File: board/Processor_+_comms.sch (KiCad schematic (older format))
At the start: 38 parts, among them U11 ATXMEGA256A3U-MH, U12 NTS0104, U14 TC1015-3.3VCT713

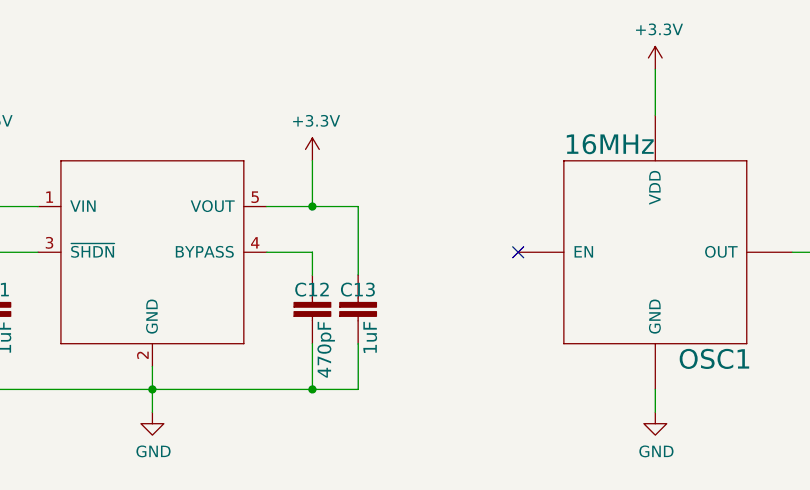
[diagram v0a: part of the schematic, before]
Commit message: Added testpoints and fixed up some issues with footprints etc
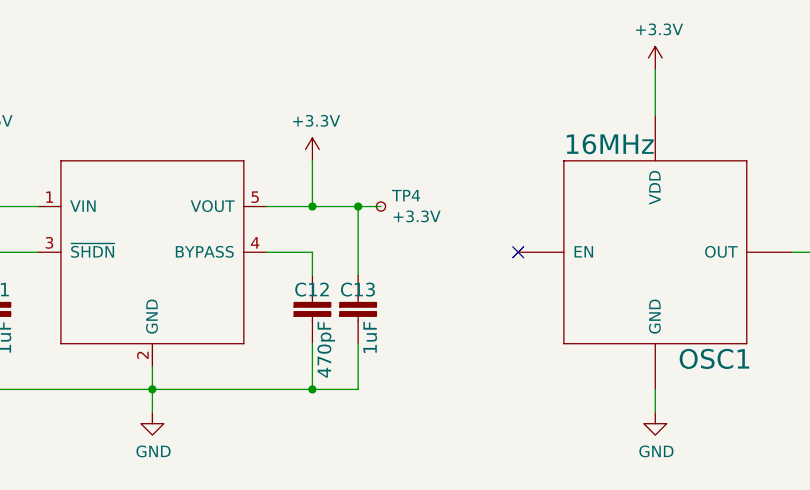
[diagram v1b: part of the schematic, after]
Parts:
- added TP4: +3.3V, TestPoint:TestPoint_Pad_D1.5mm, symbol Connector:TestPoint_Small
- C11, C13: URL https://uk.farnell.com/multicomp/mc0603x105k100ct/cap-1-f-1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 -> (none); URL_FARNELL (none) -> https://uk.farnell.com/multicomp/mc0603x105k100ct/cap-1-f-1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
- C12: URL https://uk.farnell.com/multicomp/mc0603b471j500ct/cap-470pf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 -> (none); URL_FARNELL (none) -> https://uk.farnell.com/multicomp/mc0603b471j500ct/cap-470pf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
- OSC1: URL http://uk.farnell.com/iqd-frequency-products/lfspxo025494/o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 -> (none); URL_FARNELL (none) -> http://uk.farnell.com/iqd-frequency-products/lfspxo025494/o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
- R17, R19: URL https://uk.farnell.com/vishay/crcw08051m00fkea/res-1m-1-0-1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 -> (none); URL_FARNELL (none) -> https://uk.farnell.com/vishay/crcw08051m00fkea/res-1m-1-0-1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
- U14: footprint MXKeyboard_RGB:SOT23-5L -> Package_TO_SOT_SMD:SOT-23-5
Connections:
- net +3V3: now also TP4.1
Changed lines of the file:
@@
 F 5 "CRCW08051M00FKEA" H 9700 5950 59  0001 L BNN "MPN"
 F 6 "1652946" H 9700 5950 59  0001 L BNN "OC_FARNELL"
-F 7 "https://uk.farnell.com/vishay/crcw08051m00fkea/res-1m-1-0-125w-0805-thick-film/dp/1652946" H 9700 5950 59  0001 L BNN "URL"
+F 7 "" H 9700 5950 59  0001 L BNN "URL"
+F 8 "https://uk.farnell.com/vishay/crcw08051m00fkea/res-1m-1-0-125w-0805-thick-film/dp/1652946" H 9700 5950 50  0001 C CNN "URL_FARNELL"
 	1    9700 5950
 	0    -1   -1   0
@@
 F 5 "CRCW08051M00FKEA" H 14300 7400 59  0001 L BNN "MPN"
 F 6 "1652946" H 14300 7400 59  0001 L BNN "OC_FARNELL"
-F 7 "https://uk.farnell.com/vishay/crcw08051m00fkea/res-1m-1-0-125w-0805-thick-film/dp/1652946" H 14300 7400 59  0001 L BNN "URL"
+F 7 "" H 14300 7400 59  0001 L BNN "URL"
+F 8 "https://uk.farnell.com/vishay/crcw08051m00fkea/res-1m-1-0-125w-0805-thick-film/dp/1652946" H 14300 7400 50  0001 C CNN "URL_FARNELL"
 	1    14300 7400
 	1    0    0    -1
@@
 F 0 "U14" H 7700 2200 50  0001 C CNN
 F 1 "TC1015-3.3VCT713" H 7700 2200 50  0001 C CNN
-F 2 "MXKeyboard_RGB:SOT23-5L" H 7700 2200 50  0001 C CNN
+F 2 "Package_TO_SOT_SMD:SOT-23-5" H 7700 2200 50  0001 C CNN
 F 3 "" H 7700 2200 50  0001 C CNN
 	1    7700 2200
@@
 F 5 "MC0603X105K100CT" H 7000 2400 59  0001 L BNN "MPN"
 F 6 "1759399" H 7000 2400 59  0001 L BNN "OC_FARNELL"
-F 7 "https://uk.farnell.com/multicomp/mc0603x105k100ct/cap-1-f-10v-10-x5r-0603/dp/1759399" H 7000 2400 59  0001 L BNN "URL"
+F 7 "" H 7000 2400 59  0001 L BNN "URL"
+F 8 "https://uk.farnell.com/multicomp/mc0603x105k100ct/cap-1-f-10v-10-x5r-0603/dp/1759399" H 7000 2400 50  0001 C CNN "URL_FARNELL"
 	1    7000 2400
 	1    0    0    -1
@@
 F 5 "MC0603B471J500CT" H 8400 2400 59  0001 L BNN "MPN"
 F 6 "2627442" H 8400 2400 59  0001 L BNN "OC_FARNELL"
-F 7 "https://uk.farnell.com/multicomp/mc0603b471j500ct/cap-470pf-50v-5-x7r-0603/dp/2627442" H 8400 2400 59  0001 L BNN "URL"
+F 7 "" H 8400 2400 59  0001 L BNN "URL"
+F 8 "https://uk.farnell.com/multicomp/mc0603b471j500ct/cap-470pf-50v-5-x7r-0603/dp/2627442" H 8400 2400 50  0001 C CNN "URL_FARNELL"
 	1    8400 2400
 	1    0    0    -1
@@
 F 5 "MC0603X105K100CT" H 8600 2400 59  0001 L BNN "MPN"
 F 6 "1759399" H 8600 2400 59  0001 L BNN "OC_FARNELL"
-F 7 "https://uk.farnell.com/multicomp/mc0603x105k100ct/cap-1-f-10v-10-x5r-0603/dp/1759399" H 8600 2400 59  0001 L BNN "URL"
+F 7 "" H 8600 2400 59  0001 L BNN "URL"
+F 8 "https://uk.farnell.com/multicomp/mc0603x105k100ct/cap-1-f-10v-10-x5r-0603/dp/1759399" H 8600 2400 50  0001 C CNN "URL_FARNELL"
 	1    8600 2400
 	1    0    0    -1
@@
 F 9 "LFSPXO025494" H 9900 2200 85  0001 L BNN "MPN"
 F 10 "2449455" H 9900 2200 85  0001 L BNN "OC_FARNELL"
-F 11 "http://uk.farnell.com/iqd-frequency-products/lfspxo025494/oscillator-16mhz-15pf-smd/dp/2449455" H 9900 2200 85  0001 L BNN "URL"
+F 11 "" H 9900 2200 85  0001 L BNN "URL"
+F 12 "http://uk.farnell.com/iqd-frequency-products/lfspxo025494/oscillator-16mhz-15pf-smd/dp/2449455" H 9900 2200 50  0001 C CNN "URL_FARNELL"
 	1    9900 2200
 	1    0    0    -1
@@
 	-1   0    0    1
 $EndComp
+$Comp
+L Connector:TestPoint_Small TP4
+U 1 1 5F711D45
+P 8700 2000
+F 0 "TP4" H 8748 2046 50  0000 L CNN
+F 1 "+3.3V" H 8748 1955 50  0000 L CNN
+F 2 "TestPoint:TestPoint_Pad_D1.5mm" H 8900 2000 50  0001 C CNN
+F 3 "~" H 8900 2000 50  0001 C CNN
+	1    8700 2000
+	1    0    0    -1
+$EndComp
+Wire Wire Line
+	8700 2000 8600 2000
+Connection ~ 8600 2000
 Wire Bus Line
 	4350 4400 4350 4800

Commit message: Updated the footprints in the schematic having renamed all of my published libraries
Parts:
- C1, C11, C12, C13, C2, C3, C4, C5, C6, C7, C8, C9: footprint rcl:C0603 -> rhais_rcl:C0603
- R17, R18, R19, R37, R38: footprint rcl:R0603 -> rhais_rcl:R0603
- U14: footprint Package_TO_SOT_SMD:SOT-23-5 -> rhais_package-smd:SOT-23-5
- USB: footprint USB:MICRO-USB-B-(IN_PCB) -> rhais_usb:MICRO-USB-B-(IN_PCB)
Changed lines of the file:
@@
 F 0 "USB1" H 10000 5550 59  0000 R CNN
 F 1 "USB" H 10000 4850 59  0000 R CNN
-F 2 "USB:MICRO-USB-B-(IN_PCB)" H 9850 5200 50  0001 C CNN
+F 2 "rhais_usb:MICRO-USB-B-(IN_PCB)" H 9850 5200 50  0001 C CNN
 F 3 "" H 9850 5200 50  0001 C CNN
 	1    9850 5200
@@
 F 0 "C1" H 10010 5915 59  0000 L BNN
 F 1 "0.1uF" H 10010 5715 59  0000 L BNN
-F 2 "rcl:C0603" H 9950 5900 50  0001 C CNN
+F 2 "rhais_rcl:C0603" H 9950 5900 50  0001 C CNN
 F 3 "" H 9950 5900 50  0001 C CNN
 F 4 "Multicomp" H 9950 5900 59  0001 L BNN "MFR"
@@
 F 0 "R17" H 9700 6000 59  0000 C BNN
 F 1 "1M" H 9700 5900 59  0000 C TNN
-F 2 "rcl:R0603" H 9700 5950 50  0001 C CNN
+F 2 "rhais_rcl:R0603" H 9700 5950 50  0001 C CNN
 F 3 "" H 9700 5950 50  0001 C CNN
 F 4 "Vishay" H 9700 5950 59  0001 L BNN "MFR"
@@
 F 0 "C2" H 5300 2100 59  0000 C BNN
 F 1 "0.1uF" V 5320 2000 59  0000 R TNN
-F 2 "rcl:C0603" H 5300 2100 50  0001 C CNN
+F 2 "rhais_rcl:C0603" H 5300 2100 50  0001 C CNN
 F 3 "" H 5300 2100 50  0001 C CNN
 F 4 "Multicomp" H 5300 2100 59  0001 L BNN "MFR"
@@
 F 0 "C3" H 5500 2100 59  0000 C BNN
 F 1 "0.1uF" V 5520 2000 59  0000 R TNN
-F 2 "rcl:C0603" H 5500 2100 50  0001 C CNN
+F 2 "rhais_rcl:C0603" H 5500 2100 50  0001 C CNN
 F 3 "" H 5500 2100 50  0001 C CNN
 F 4 "Multicomp" H 5500 2100 59  0001 L BNN "MFR"
@@
 F 0 "C4" H 5700 2100 59  0000 C BNN
 F 1 "0.1uF" V 5720 2000 59  0000 R TNN
-F 2 "rcl:C0603" H 5700 2100 50  0001 C CNN
+F 2 "rhais_rcl:C0603" H 5700 2100 50  0001 C CNN
 F 3 "" H 5700 2100 50  0001 C CNN
 F 4 "Multicomp" H 5700 2100 59  0001 L BNN "MFR"
@@
 F 0 "C5" H 5900 2100 59  0000 C BNN
 F 1 "0.1uF" V 5920 2000 59  0000 R TNN
-F 2 "rcl:C0603" H 5900 2100 50  0001 C CNN
+F 2 "rhais_rcl:C0603" H 5900 2100 50  0001 C CNN
 F 3 "" H 5900 2100 50  0001 C CNN
 F 4 "Multicomp" H 5900 2100 59  0001 L BNN "MFR"
@@
 F 0 "C6" H 6100 2100 59  0000 C BNN
 F 1 "0.1uF" V 6120 2000 59  0000 R TNN
-F 2 "rcl:C0603" H 6100 2100 50  0001 C CNN
+F 2 "rhais_rcl:C0603" H 6100 2100 50  0001 C CNN
 F 3 "" H 6100 2100 50  0001 C CNN
 F 4 "Multicomp" H 6100 2100 59  0001 L BNN "MFR"
@@
 F 0 "R18" H 4800 4150 59  0000 C BNN
 F 1 "10k" H 4800 4050 59  0000 C TNN
-F 2 "rcl:R0603" H 4800 4100 50  0001 C CNN
+F 2 "rhais_rcl:R0603" H 4800 4100 50  0001 C CNN
 F 3 "" H 4800 4100 50  0001 C CNN
 F 4 "Multicomp" H 4800 4100 59  0001 L BNN "MFR"
@@
 F 0 "R19" H 14300 7450 59  0000 C BNN
 F 1 "1M" H 14300 7350 59  0000 C TNN
-F 2 "rcl:R0603" H 14300 7400 50  0001 C CNN
+F 2 "rhais_rcl:R0603" H 14300 7400 50  0001 C CNN
 F 3 "" H 14300 7400 50  0001 C CNN
 F 4 "Vishay" H 14300 7400 59  0001 L BNN "MFR"
@@
 F 0 "C7" V 14315 7090 59  0000 L TNN
 F 1 "0.1uF" V 14315 6990 59  0000 R TNN
-F 2 "rcl:C0603" H 14250 7100 50  0001 C CNN
+F 2 "rhais_rcl:C0603" H 14250 7100 50  0001 C CNN
 F 3 "" H 14250 7100 50  0001 C CNN
 F 4 "Multicomp" H 14250 7100 59  0001 L BNN "MFR"
@@
 F 0 "C8" H 13560 5815 59  0000 L BNN
 F 1 "0.1uF" H 13560 5615 59  0000 L BNN
-F 2 "rcl:C0603" H 13500 5800 50  0001 C CNN
+F 2 "rhais_rcl:C0603" H 13500 5800 50  0001 C CNN
 F 3 "" H 13500 5800 50  0001 C CNN
 F 4 "Multicomp" H 13500 5800 59  0001 L BNN "MFR"
@@
 F 0 "C9" H 12160 5815 59  0000 L BNN
 F 1 "0.1uF" H 12160 5615 59  0000 L BNN
-F 2 "rcl:C0603" H 12100 5800 50  0001 C CNN
+F 2 "rhais_rcl:C0603" H 12100 5800 50  0001 C CNN
 F 3 "" H 12100 5800 50  0001 C CNN
 F 4 "Multicomp" H 12100 5800 59  0001 L BNN "MFR"
@@
 F 0 "U14" H 7700 2200 50  0001 C CNN
 F 1 "TC1015-3.3VCT713" H 7700 2200 50  0001 C CNN
-F 2 "Package_TO_SOT_SMD:SOT-23-5" H 7700 2200 50  0001 C CNN
+F 2 "rhais_package-smd:SOT-23-5" H 7700 2200 50  0001 C CNN
 F 3 "" H 7700 2200 50  0001 C CNN
 	1    7700 2200
@@
 F 0 "C11" H 7000 2400 59  0000 C BNN
 F 1 "1uF" V 7020 2300 59  0000 R TNN
-F 2 "rcl:C0603" H 7000 2400 50  0001 C CNN
+F 2 "rhais_rcl:C0603" H 7000 2400 50  0001 C CNN
 F 3 "" H 7000 2400 50  0001 C CNN
 F 4 "Multicomp" H 7000 2400 59  0001 L BNN "MFR"
@@
 F 0 "C12" H 8400 2400 59  0000 C BNN
 F 1 "470pF" V 8420 2300 59  0000 R TNN
-F 2 "rcl:C0603" H 8400 2400 50  0001 C CNN
+F 2 "rhais_rcl:C0603" H 8400 2400 50  0001 C CNN
 F 3 "" H 8400 2400 50  0001 C CNN
 F 4 "Multicomp" H 8400 2400 59  0001 L BNN "MFR"
@@
 F 0 "C13" H 8600 2400 59  0000 C BNN
 F 1 "1uF" V 8620 2300 59  0000 R TNN
-F 2 "rcl:C0603" H 8600 2400 50  0001 C CNN
+F 2 "rhais_rcl:C0603" H 8600 2400 50  0001 C CNN
 F 3 "" H 8600 2400 50  0001 C CNN
 F 4 "Multicomp" H 8600 2400 59  0001 L BNN "MFR"
@@
 F 0 "R37" H 9300 5800 59  0000 C BNN
 F 1 "100k" H 9300 5700 59  0000 C TNN
-F 2 "rcl:R0603" H 9300 5750 50  0001 C CNN
+F 2 "rhais_rcl:R0603" H 9300 5750 50  0001 C CNN
 F 3 "" H 9300 5750 50  0001 C CNN
 	1    9300 5750
@@
 F 0 "R38" V 9450 4500 50  0000 C BNN
 F 1 "10k" V 9550 4500 50  0000 C TNN
-F 2 "rcl:R0603" H 9500 4500 50  0001 C CNN
+F 2 "rhais_rcl:R0603" H 9500 4500 50  0001 C CNN
 F 3 "" H 9500 4500 50  0001 C CNN
 F 4 "Multicomp" H 9500 4500 50  0001 C CNN "MFR"

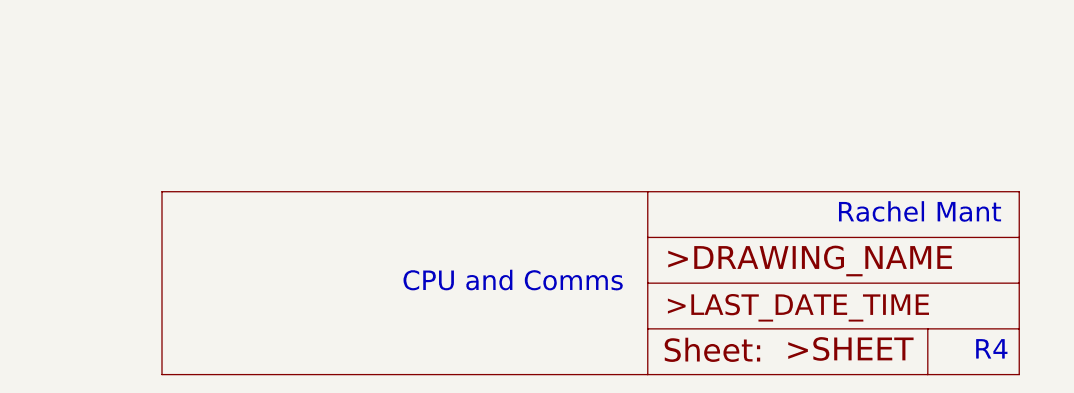
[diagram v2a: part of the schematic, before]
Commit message: Fixed up the schematics metadata to properly capture revision, block and authorship information
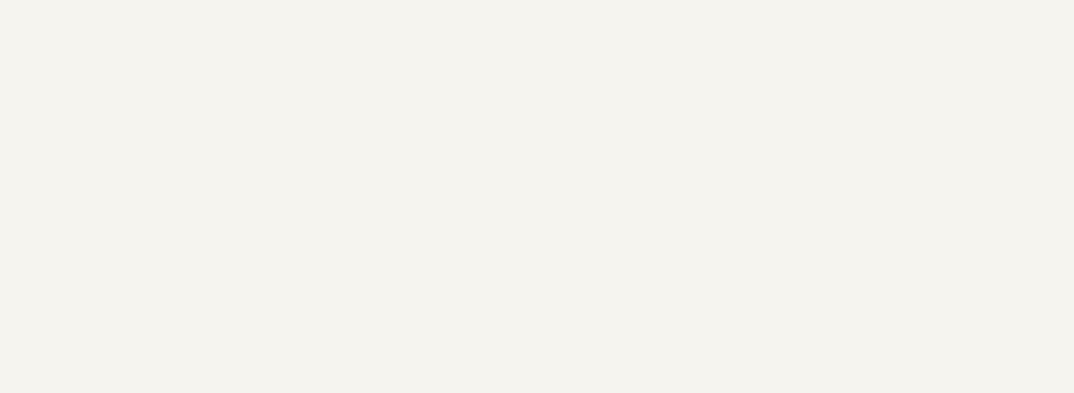
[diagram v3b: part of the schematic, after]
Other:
- note removed: "CPU and Comms"
- note removed: "R4"
- note removed: "Rachel Mant"
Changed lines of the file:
@@
 encoding utf-8
 Sheet 6 6
-Title ""
+Title "CPU and Comms"
 Date ""
-Rev ""
-Comp ""
+Rev "4"
+Comp "Rachel Mant"
 Comment1 ""
 Comment2 ""
@@
 $EndComp
 $Comp
-L MXKeyboard_RGB-eagle-import:A3L-LOC #FRAME1
-U 1 1 73DA64CA
-P 900 10300
-AR Path="/73DA64CA" Ref="#FRAME1"  Part="1"
-AR Path="/5F5D6257/73DA64CA" Ref="#FRAME1"  Part="1"
-F 0 "#FRAME1" H 900 10300 50  0001 C CNN
-F 1 "A3L-LOC" H 900 10300 50  0001 C CNN
-F 2 "" H 900 10300 50  0001 C CNN
-F 3 "" H 900 10300 50  0001 C CNN
-	1    900  10300
-	1    0    0    -1
-$EndComp
-$Comp
 L MXKeyboard_RGB-eagle-import:R-EU_R0603 R37
 U 1 1 B80E1D1D
@@
 	0    -1   -1   0
 $EndComp
-Text Notes 13300 9800 0    85   ~ 0
-CPU and Comms
-Text Notes 15800 10100 0    85   ~ 0
-R4
-Text Notes 15200 9500 0    85   ~ 0
-Rachel Mant
 Text HLabel 4400 6500 0    50   Output ~ 0
 SCLK_GREEN

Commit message: Fixed up a few more resistors that were still using the eagle import library versions of their schematic symbols
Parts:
- R17, R19: symbol MXKeyboard_RGB-eagle-import:R-EU_R0805 -> Device:R_Small
- R18, R37: symbol MXKeyboard_RGB-eagle-import:R-EU_R0603 -> Device:R_Small
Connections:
- net +3V3: now also R18.2; no longer R18.1
- net EARTH_PS/2: now also R19.1; no longer R19.2
- net EARTH_USB: now also R17.1; no longer R17.2
- net GND: now also R17.2, R19.2, R37.2; no longer R17.1, R19.1, R37.1
- net ~RESET: now also R18.1; no longer R18.2
- net at U11.36 (PE0), USB.ID: now also R37.1; no longer R37.2
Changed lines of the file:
@@
 	9950 6200 9950 6100
 Wire Wire Line
-	9700 6150 9700 6200
-Wire Wire Line
-	9300 5950 9300 6200
+	9700 6050 9700 6200
+Wire Wire Line
+	9300 5850 9300 6200
 Wire Wire Line
 	9300 6200 9500 6200
@@
 	14000 7100 14000 7400
 Wire Wire Line
-	14000 7400 14100 7400
+	14000 7400 14200 7400
 Wire Wire Line
 	14150 7100 14000 7100
@@
 	9950 5700 10050 5700
 Wire Wire Line
-	9700 5750 9700 5700
+	9700 5850 9700 5700
 Connection ~ 9950 5700
 Text Label 10050 5700 0    50   ~ 0
@@
 	5100 4200 5100 4100
 Wire Wire Line
-	5100 4100 5000 4100
+	5100 4100 4900 4100
 Wire Wire Line
 	5100 4100 5100 4000
@@
 	4500 4000 4500 4100
 Wire Wire Line
-	4500 4100 4600 4100
+	4500 4100 4700 4100
 Wire Wire Line
 	12600 5500 12600 5600
@@
 	14600 7100 14600 7400
 Wire Wire Line
-	14600 7400 14500 7400
+	14600 7400 14400 7400
 Wire Wire Line
 	14450 7100 14600 7100
@@
 	7000 5400 6900 5400
 Wire Wire Line
-	9300 5300 9300 5550
+	9300 5300 9300 5650
 Connection ~ 9300 5300
 Entry Wire Line
@@
 $EndComp
 $Comp
-L MXKeyboard_RGB-eagle-import:R-EU_R0805 R17
-U 1 1 063E4601
-P 9700 5950
-AR Path="/063E4601" Ref="R17"  Part="1"
-AR Path="/5F5D6257/063E4601" Ref="R17"  Part="1"
-F 0 "R17" H 9700 6000 59  0000 C BNN
-F 1 "1M" H 9700 5900 59  0000 C TNN
-F 2 "rhais_rcl:R0603" H 9700 5950 50  0001 C CNN
-F 3 "" H 9700 5950 50  0001 C CNN
-F 4 "Vishay" H 9700 5950 59  0001 L BNN "MFR"
-F 5 "CRCW08051M00FKEA" H 9700 5950 59  0001 L BNN "MPN"
-F 6 "1652946" H 9700 5950 59  0001 L BNN "OC_FARNELL"
-F 7 "" H 9700 5950 59  0001 L BNN "URL"
-F 8 "https://uk.farnell.com/vishay/crcw08051m00fkea/res-1m-1-0-125w-0805-thick-film/dp/1652946" H 9700 5950 50  0001 C CNN "URL_FARNELL"
-	1    9700 5950
-	0    -1   -1   0
-$EndComp
-$Comp
 L MXKeyboard_RGB-eagle-import:PINHD-2X5 JP1
 U 1 1 2F430EF2
@@
 $EndComp
 $Comp
-L MXKeyboard_RGB-eagle-import:R-EU_R0603 R18
+L Device:R_Small R18
 U 1 1 6A070FAE
 P 4800 4100
 AR Path="/6A070FAE" Ref="R18"  Part="1"
 AR Path="/5F5D6257/6A070FAE" Ref="R18"  Part="1"
-F 0 "R18" H 4800 4150 59  0000 C BNN
-F 1 "10k" H 4800 4050 59  0000 C TNN
+F 0 "R18" V 4750 4100 59  0000 C BNN
+F 1 "10k" V 4850 4100 59  0000 C TNN
 F 2 "rhais_rcl:R0603" H 4800 4100 50  0001 C CNN
 F 3 "" H 4800 4100 50  0001 C CNN
@@
 F 6 "2130939" H 4800 4100 59  0001 L BNN "OC_FARNELL"
 	1    4800 4100
-	1    0    0    -1
+	0    1    1    0
 $EndComp
 $Comp
@@
 $EndComp
 $Comp
-L MXKeyboard_RGB-eagle-import:R-EU_R0805 R19
+L Device:R_Small R19
 U 1 1 B4133811
 P 14300 7400
 AR Path="/B4133811" Ref="R19"  Part="1"
 AR Path="/5F5D6257/B4133811" Ref="R19"  Part="1"
-F 0 "R19" H 14300 7450 59  0000 C BNN
-F 1 "1M" H 14300 7350 59  0000 C TNN
+F 0 "R19" V 14250 7400 59  0000 C BNN
+F 1 "1M" V 14350 7400 59  0000 C TNN
 F 2 "rhais_rcl:R0603" H 14300 7400 50  0001 C CNN
 F 3 "" H 14300 7400 50  0001 C CNN
@@
 F 8 "https://uk.farnell.com/vishay/crcw08051m00fkea/res-1m-1-0-125w-0805-thick-film/dp/1652946" H 14300 7400 50  0001 C CNN "URL_FARNELL"
 	1    14300 7400
-	1    0    0    -1
+	0    1    1    0
 $EndComp
 $Comp
@@
 $EndComp
 $Comp
-L MXKeyboard_RGB-eagle-import:R-EU_R0603 R37
+L Device:R_Small R37
 U 1 1 B80E1D1D
 P 9300 5750
 AR Path="/B80E1D1D" Ref="R37"  Part="1"
 AR Path="/5F5D6257/B80E1D1D" Ref="R37"  Part="1"
-F 0 "R37" H 9300 5800 59  0000 C BNN
-F 1 "100k" H 9300 5700 59  0000 C TNN
+F 0 "R37" V 9250 5750 59  0000 C BNN
+F 1 "100k" V 9350 5750 59  0000 C TNN
 F 2 "rhais_rcl:R0603" H 9300 5750 50  0001 C CNN
 F 3 "" H 9300 5750 50  0001 C CNN
 	1    9300 5750
-	0    -1   -1   0
+	1    0    0    -1
 $EndComp
 Text HLabel 4400 6500 0    50   Output ~ 0
@@
 	8700 2000 8600 2000
 Connection ~ 8600 2000
+$Comp
+L Device:R_Small R17
+U 1 1 063E4601
+P 9700 5950
+AR Path="/063E4601" Ref="R17"  Part="1"
+AR Path="/5F5D6257/063E4601" Ref="R17"  Part="1"
+F 0 "R17" V 9650 5950 59  0000 C BNN
+F 1 "1M" V 9750 5950 59  0000 C TNN
+F 2 "rhais_rcl:R0603" H 9700 5950 50  0001 C CNN
+F 3 "" H 9700 5950 50  0001 C CNN
+F 4 "Vishay" H 9700 5950 59  0001 L BNN "MFR"
+F 5 "CRCW08051M00FKEA" H 9700 5950 59  0001 L BNN "MPN"
+F 6 "1652946" H 9700 5950 59  0001 L BNN "OC_FARNELL"
+F 7 "" H 9700 5950 59  0001 L BNN "URL"
+F 8 "https://uk.farnell.com/vishay/crcw08051m00fkea/res-1m-1-0-125w-0805-thick-film/dp/1652946" H 9700 5950 50  0001 C CNN "URL_FARNELL"
+	1    9700 5950
+	1    0    0    -1
+$EndComp
 Wire Bus Line
 	4350 4400 4350 4800
